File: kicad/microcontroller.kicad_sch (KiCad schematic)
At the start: 12 parts, among them Q701 2N7002, U701 STM32WB55RGVx, Y701 32M

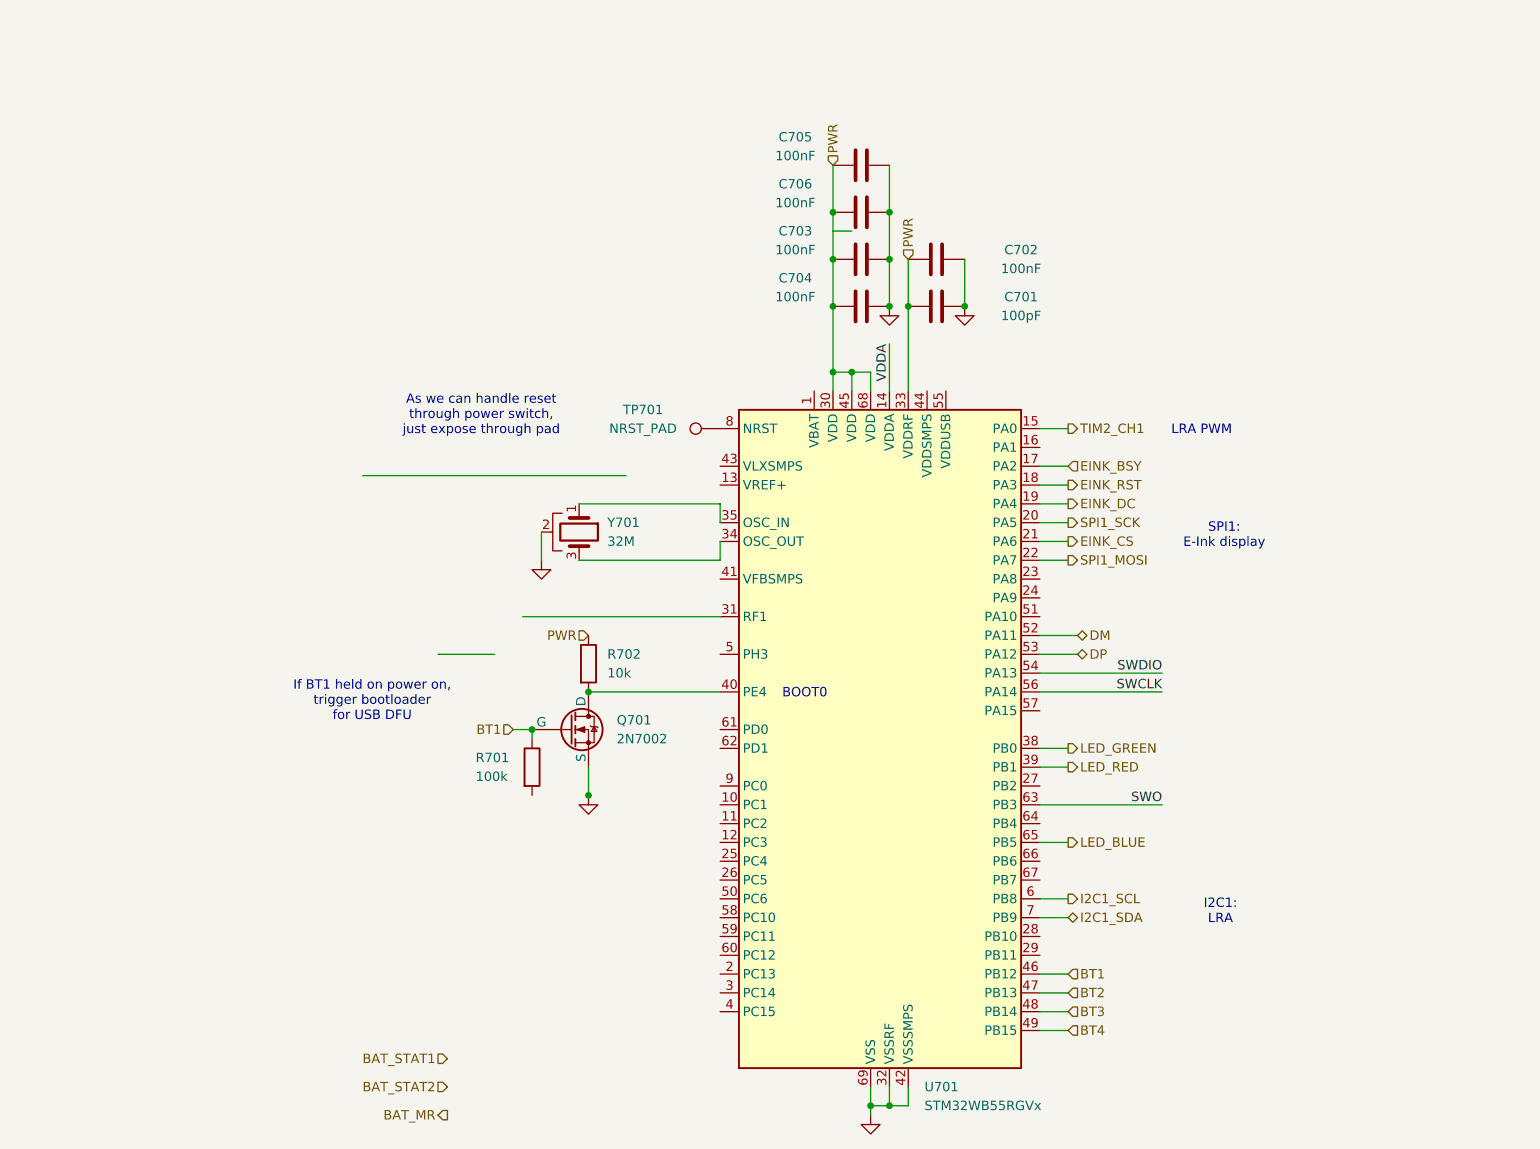
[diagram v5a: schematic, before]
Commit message: Finish microcontroller power supply
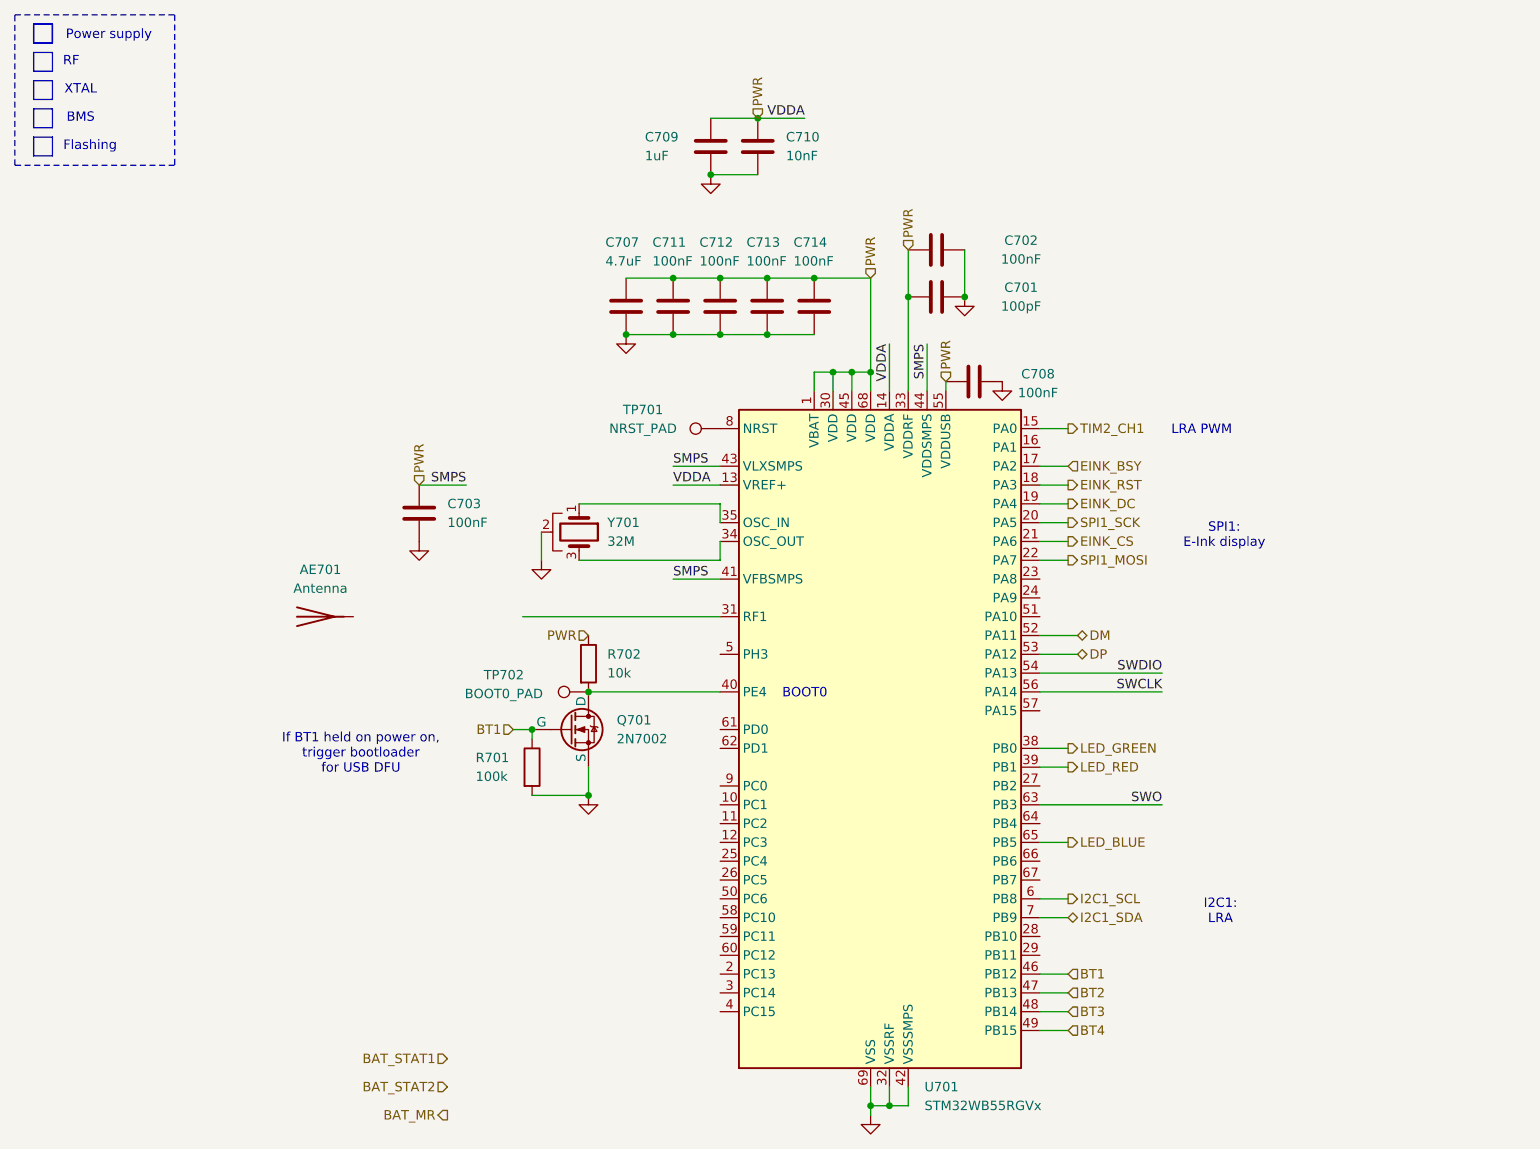
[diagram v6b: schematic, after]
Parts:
- removed C704, C705, C706: 100nF, symbol Device:C
- added AE701: Antenna, symbol Device:Antenna
- added C707: 4.7uF, symbol Device:C
- added C708, C711, C712, C713, C714: 100nF, symbol Device:C
- added C709: 1uF, symbol Device:C
- added C710: 10nF, symbol Device:C
- added TP702: BOOT0_PAD, symbol Connector:TestPoint
- C702: footprint (none) -> Capacitor_SMD:C_0603_1608Metric_Pad1.08x0.95mm_HandSolder
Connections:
- net VDDA is gone; now on net PWR: U701.14 (VDDA)
- net GND: now also R701.2, C707.2, C708.1, C709.2, C710.2, C711.2, C712.2, C713.2, C714.2
- net PWR: now also U701.1 (VBAT), U701.13 (VREF+), U701.41 (VFBSMPS), U701.43 (VLXSMPS), U701.44 (VDDSMPS), U701.55 (VDDUSB), C707.1, C708.2, C709.1, C710.1, C711.1, C712.1, C713.1, C714.1
- net at Q701.1 (D), R702.2, U701.40 (PE4): now also TP702.1
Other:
- note added: "BMS"
- note added: "Flashing"
- note added: "Power supply"
- note added: "RF"
- note added: "XTAL"
- note removed: "As we can handle reset through power switch, just expose through pad"
- moved on the sheet: C701, C702

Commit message: Microcontroller XTAL, BMS, and Flashing connections
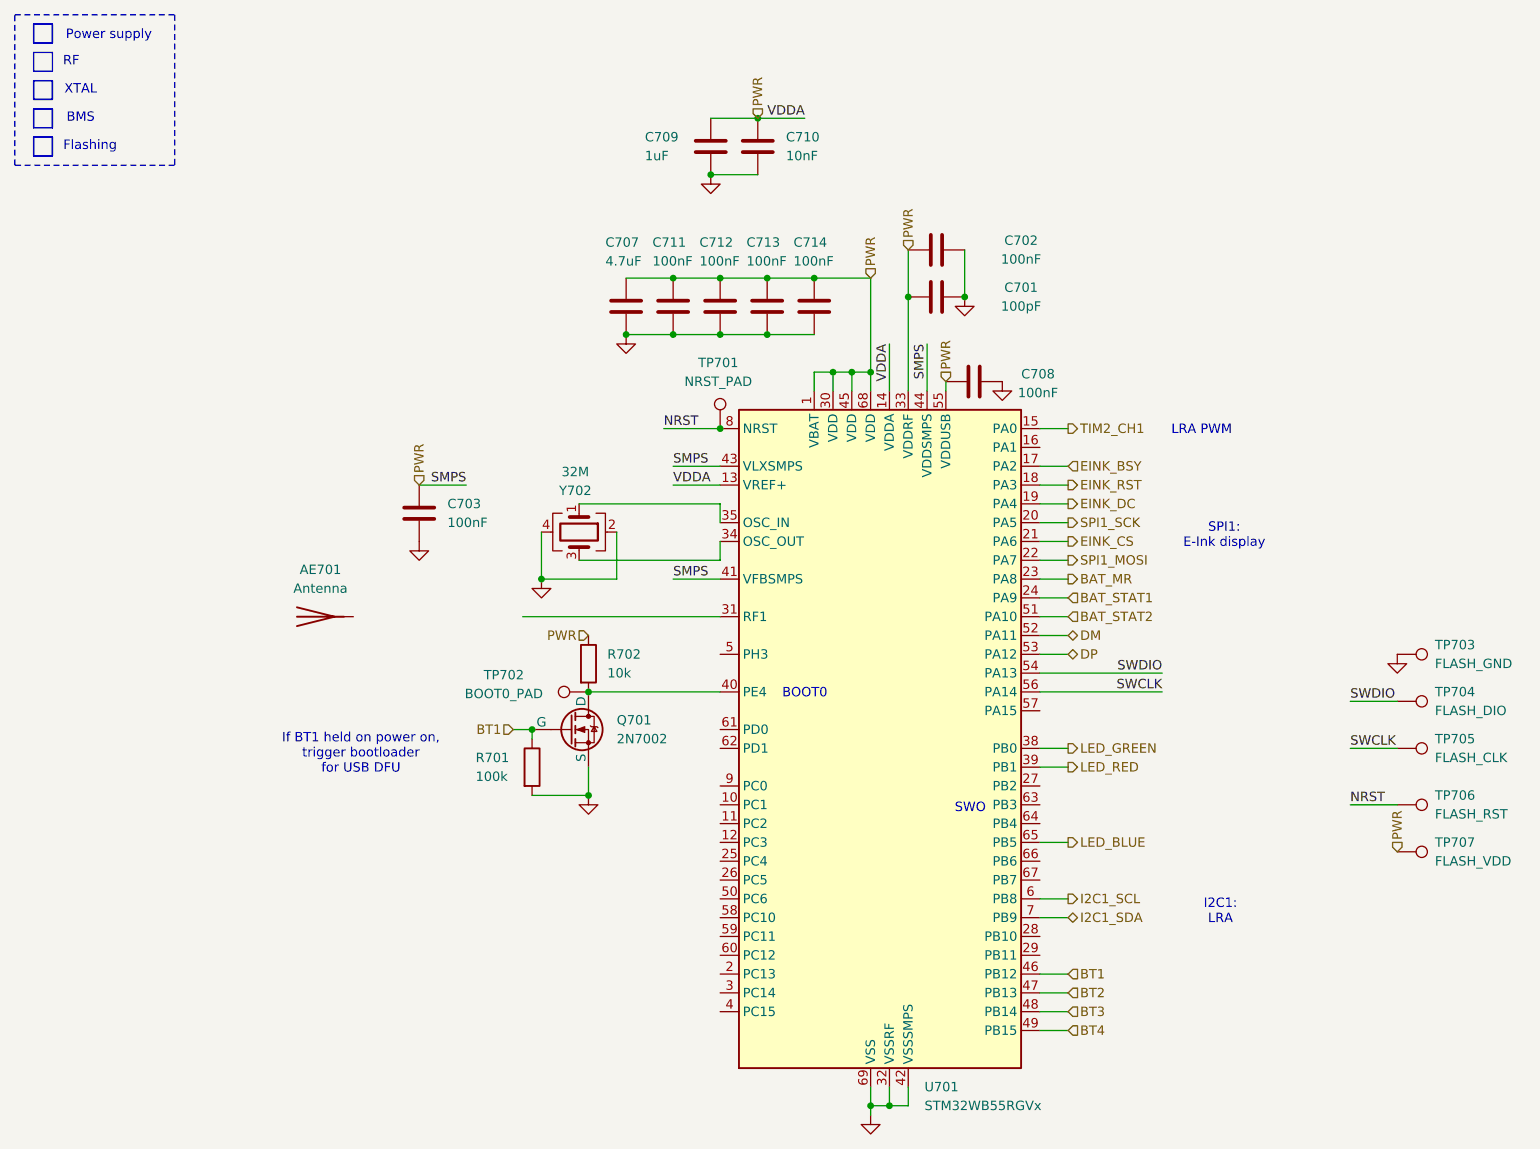
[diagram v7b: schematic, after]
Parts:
- removed Y701: 32M, symbol Device:Crystal_GND2
- added TP703: FLASH_GND, symbol Connector:TestPoint
- added TP704: FLASH_DIO, symbol Connector:TestPoint
- added TP705: FLASH_CLK, symbol Connector:TestPoint
- added TP706: FLASH_RST, symbol Connector:TestPoint
- added TP707: FLASH_VDD, symbol Connector:TestPoint
- added Y702: 32M, symbol Device:Crystal_GND24
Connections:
- net BAT_MR: now also U701.23 (PA8)
- net BAT_STAT1: now also U701.24 (PA9)
- net BAT_STAT2: now also U701.51 (PA10)
- net GND: now also TP703.1, Y702.2, Y702.4
- net PWR: now also TP707.1
- net SWCLK: now also TP705.1
- net SWDIO: now also TP704.1
- net at U701.34 (OSC_OUT): now also Y702.3
- net at U701.35 (OSC_IN): now also Y702.1
- net NRST: now reaches TP701.1, U701.8 (NRST)
- net NRST: now also TP706.1
- net SWO: no longer names the net of U701.63 (PB3)
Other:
- note added: "SWO"
- moved on the sheet: TP701

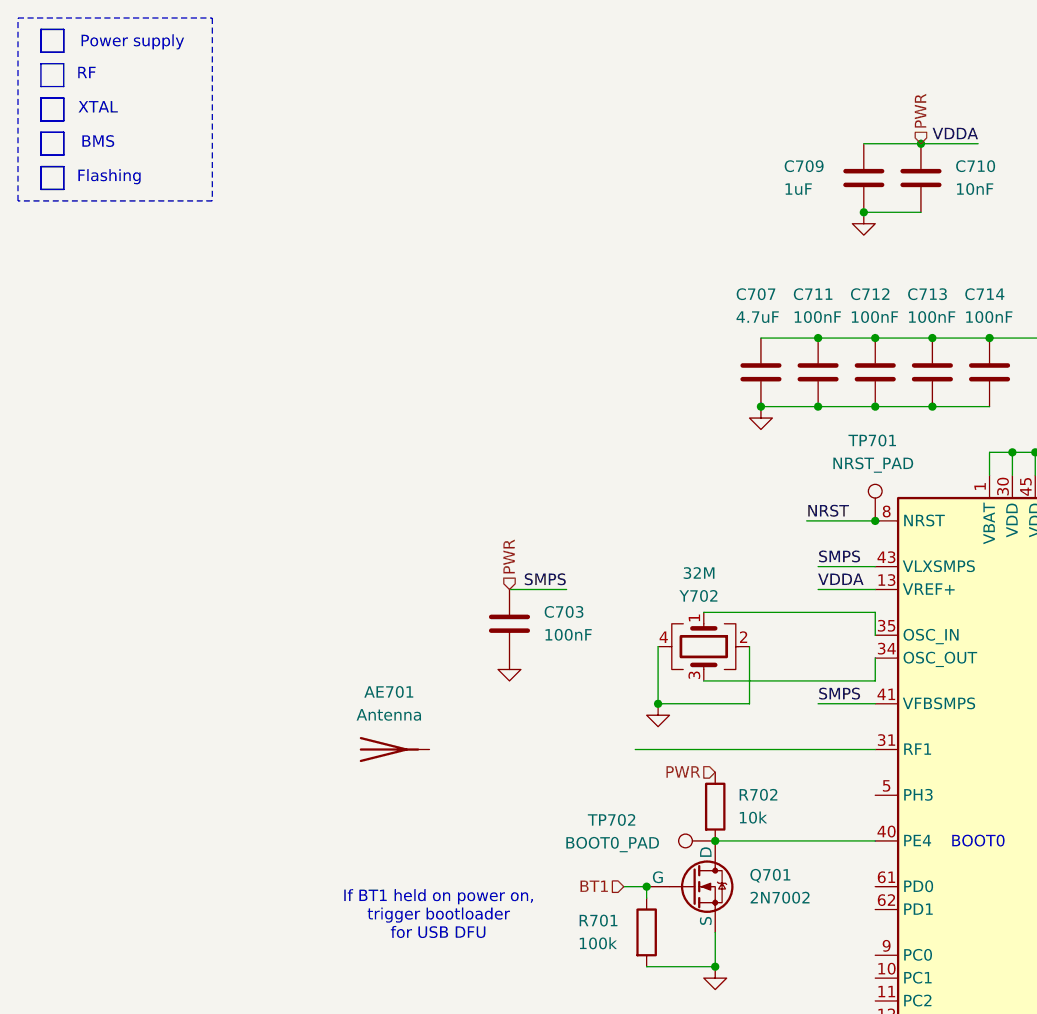
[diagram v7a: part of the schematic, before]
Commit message: Finish microcontroller, adding RF
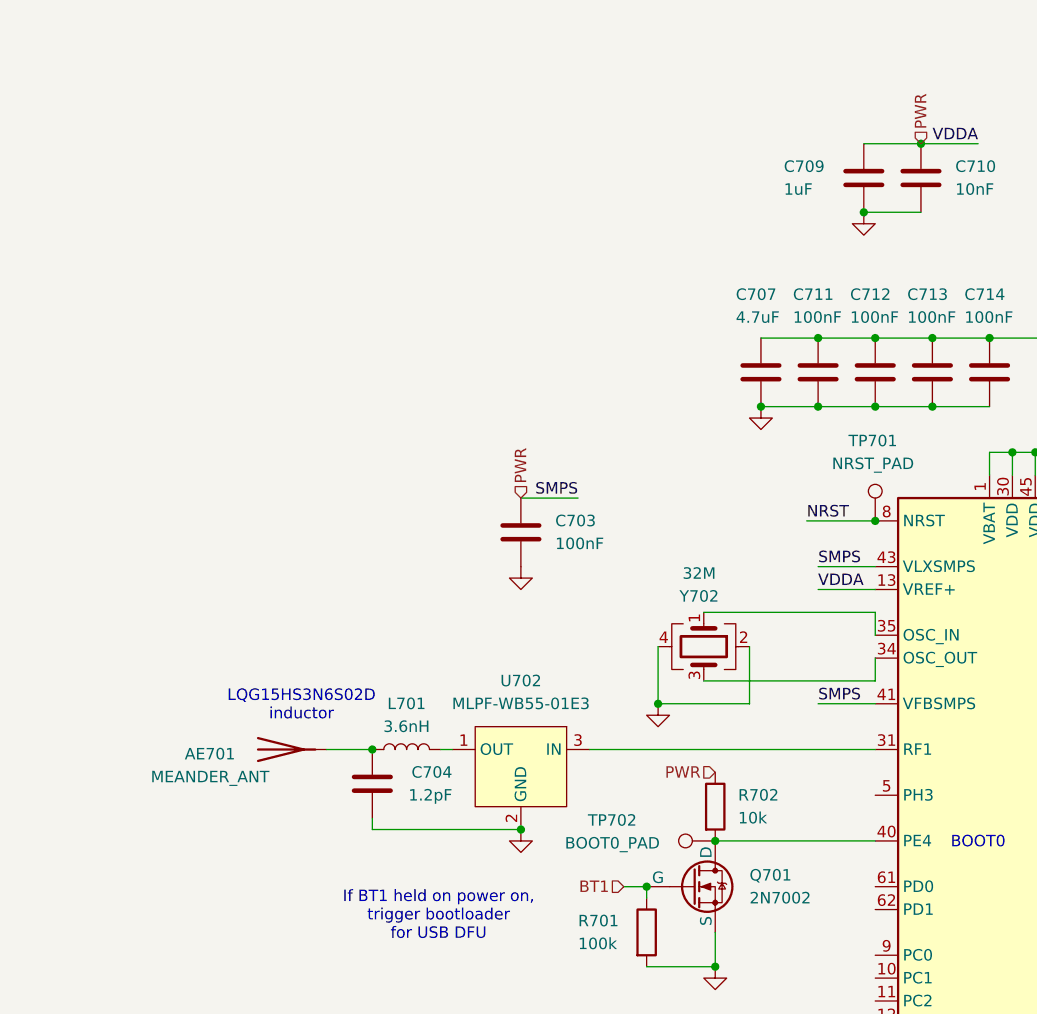
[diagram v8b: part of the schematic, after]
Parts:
- added C704: 1.2pF, symbol Device:C
- added L701: 3.6nH, Capacitor_SMD:C_0402_1005Metric_Pad0.74x0.62mm_HandSolder, symbol Device:L
- added U702: MLPF-WB55-01E3, Raven:MLPF-WB55-01E3, symbol Raven:MLPF-WB55-01E3-2
- AE701: value Antenna -> MEANDER_ANT
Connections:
- net GND: now also C704.2, U702.2 (GND), U702.4 (GND), U702.5 (GND), U702.6 (GND)
- net at U701.31 (RF1): now also U702.3 (IN)
- net at AE701.1 (A): now also C704.1, L701.1
- new net: L701.2, U702.1 (OUT)
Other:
- note added: "LQG15HS3N6S02D inductor"
- note removed: "BMS"
- note removed: "Flashing"
- note removed: "Power supply"
- note removed: "RF"
- note removed: "XTAL"
- moved on the sheet: AE701, C703
